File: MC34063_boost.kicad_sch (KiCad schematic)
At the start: 22 parts, among them U1 MC34063AP

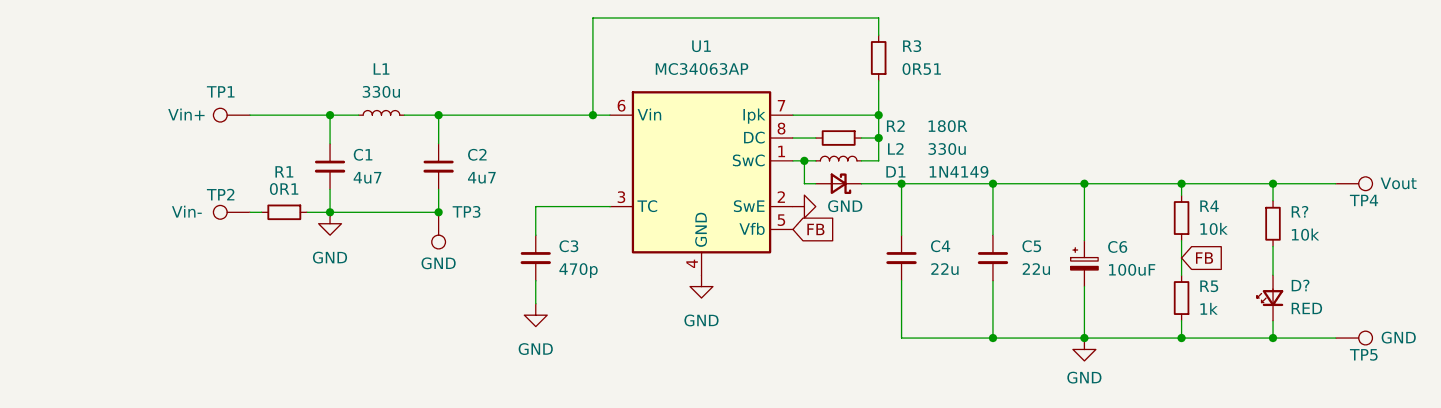
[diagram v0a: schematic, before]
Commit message: Fix: added input indicator LED
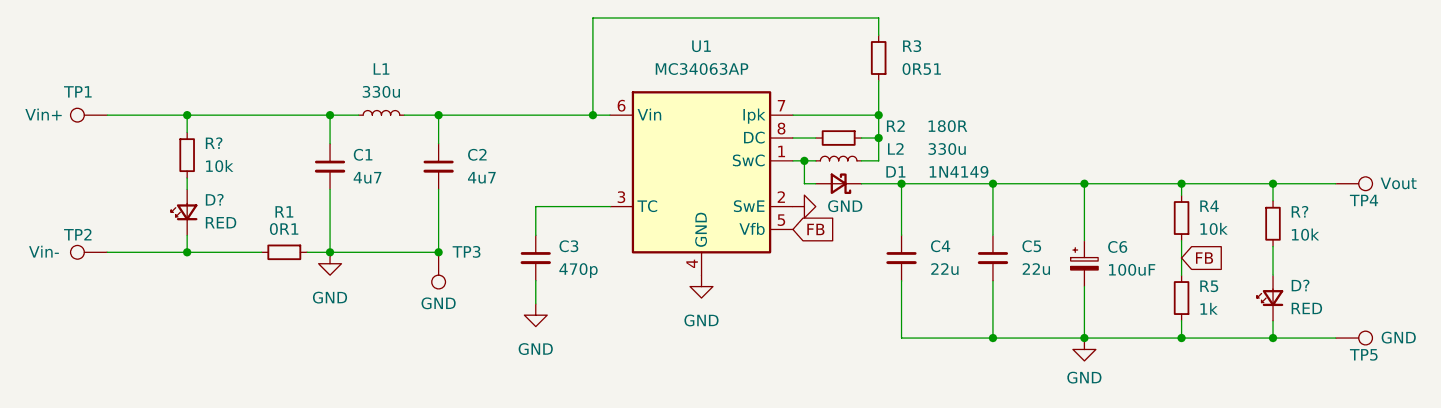
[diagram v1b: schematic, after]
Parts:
- added D?: RED, symbol Device:LED_Small
- added R?: 10k, symbol Device:R_Small
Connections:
- net at R1.2, TP2.1: now also D?.1 (K)
- net at C1.1, L1.1, TP1.1: now also R?.1
- new net: D?.2 (A), R?.2
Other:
- moved on the sheet: R1, TP1, TP2, TP3
